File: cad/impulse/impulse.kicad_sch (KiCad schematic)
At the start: 0 parts

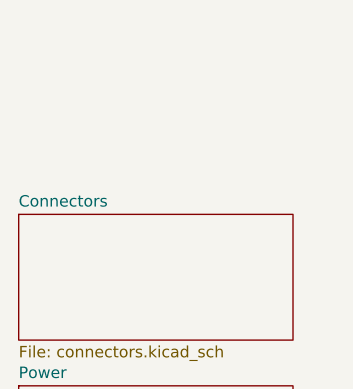
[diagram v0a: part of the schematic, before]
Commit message: Started Working on sensors. Made connectors for servos.
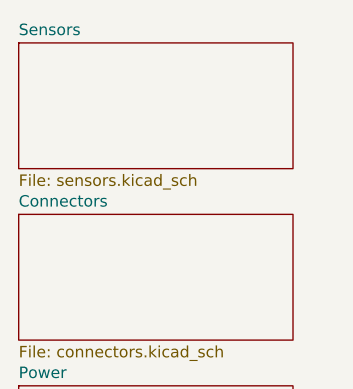
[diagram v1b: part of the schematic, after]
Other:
- added sheet Sensors (sensors.kicad_sch)
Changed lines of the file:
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@@
 (kicad_sch (version 20230121) (generator eeschema)
   (paper "A4")
+  (sheet (at 227.33 105.41) (size 30.48 13.97) (fields_autoplaced)
+    (stroke (width 0.1524) (type solid))
+    (fill (color 0 0 0 0.0000))
+    (property "Sheetname" "Sensors" (at 227.33 104.6984 0)
+      (effects (font (size 1.27 1.27)) (justify left bottom))
+    )
+    (property "Sheetfile" "sensors.kicad_sch" (at 227.33 119.9646 0)
+      (effects (font (size 1.27 1.27)) (justify left top))
+    )
+    (instances
+      (project "impulse"
+        (path "/eb4cfece-5fcb-437a-ac58-337ab6512039" (page "4"))
+      )
+    )
+  )
   (sheet (at 227.33 143.51) (size 30.48 13.97) (fields_autoplaced)
     (stroke (width 0.1524) (type solid))

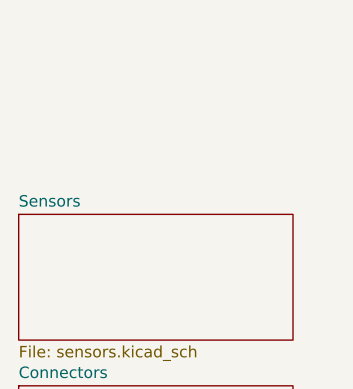
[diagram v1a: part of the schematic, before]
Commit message: Added IMU, button and led. Moved things around.
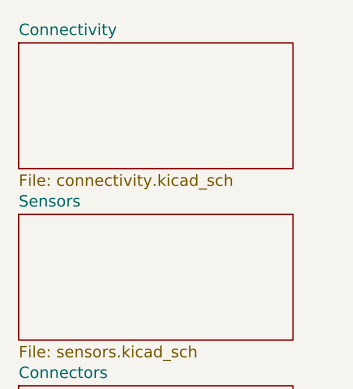
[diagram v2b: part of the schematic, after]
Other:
- added sheet Connectivity (connectivity.kicad_sch)
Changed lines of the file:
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@@
+    )
+  )
+  (sheet (at 227.33 86.36) (size 30.48 13.97) (fields_autoplaced)
+    (stroke (width 0.1524) (type solid))
+    (fill (color 0 0 0 0.0000))
+    (property "Sheetname" "Connectivity" (at 227.33 85.6484 0)
+      (effects (font (size 1.27 1.27)) (justify left bottom))
+    )
+    (property "Sheetfile" "connectivity.kicad_sch" (at 227.33 100.9146 0)
+      (effects (font (size 1.27 1.27)) (justify left top))
+    )
+    (instances
+      (project "impulse"
+        (path "/eb4cfece-5fcb-437a-ac58-337ab6512039" (page "5"))
+      )
     )
   )

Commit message: Finnished the design.
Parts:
- added C38, C39, C40, C44: 100n, symbol Device:C_Small
- added C41: 4u7, symbol Device:C_Small
- added C42: 10n, symbol Device:C_Small
- added C43, C45: 1u, symbol Device:C_Small
- added C46, C47: 10p, symbol Device:C_Small
- added J14: Conn_02x04_Counter_Clockwise, symbol Connector_Generic:Conn_02x04_Counter_Clockwise
- added R14, R15, R35, R36, R37: 0r, symbol Device:R_Small
- added U13: STM32G431CBUx, symbol MCU_ST_STM32G4:STM32G431CBUx
- added Y2: X252016MLB4SI, symbol Device:Crystal_GND24
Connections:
- new net: J14.2 (Pin_2), R14.2
- new net: J14.3 (Pin_3), R15.2
- new net: J14.5 (Pin_5), R37.1
- new net: J14.6 (Pin_6), R36.1
- new net: J14.7 (Pin_7), R35.1
- new net +3V3: C38.1, C39.1, C40.1, C41.1, C42.1, C43.1, C44.1, C45.1, J14.8 (Pin_8), U13.1 (VBAT), U13.20 (VREF+), U13.21 (VDDA), U13.23 (VDD), U13.35 (VDD), U13.48 (VDD)
- new net GND: C38.2, C39.2, C40.2, C41.2, C42.2, C43.2, C44.2, C45.2, C46.2, C47.2, J14.1 (Pin_1), J14.4 (Pin_4), U13.49 (VSS), Y2.2, Y2.4
- new net SD_cs: U13.32 (PA10)
- new net SD_miso: U13.40 (PC11)
- new net SD_mosi: U13.43 (PB5)
- new net SD_sck: U13.39 (PC10)
- new net button: R37.2, U13.7 (PG10)
- new net flash_cs: U13.25 (PB12)
- new net flash_miso: U13.27 (PB14)
- new net flash_mosi: U13.28 (PB15)
- new net flash_sck: U13.26 (PB13)
- new net fpc_gpio: U13.16 (PC4)
- new net fpc_rx: U13.24 (PB11)
- new net fpc_scl: U13.38 (PA15)
- new net fpc_sda: U13.47 (PB9)
- new net fpc_tx: U13.22 (PB10)
- new net i2c2_scl: U13.31 (PA9)
- new net i2c2_sda: U13.30 (PA8)
- new net led_b: U13.4 (PC15)
- new net led_g: U13.3 (PC14)
- new net led_r: U13.2 (PC13)
- new net pyro_0: U13.44 (PB6)
- new net pyro_1: U13.45 (PB7)
- new net pyro_2: U13.46 (PB8)
- new net pyro_3: U13.17 (PB0)
- new net servo_0: U13.8 (PA0)
- new net servo_1: U13.9 (PA1)
- new net servo_2: U13.10 (PA2)
- new net servo_3: U13.11 (PA3)
- new net servo_4: U13.29 (PC6)
- new net servo_5: U13.12 (PA4)
- new net stm_swclk: R15.1, U13.37 (PA14)
- new net stm_swdio: R14.1, U13.36 (PA13)
- new net stm_xta: C46.1, U13.5 (PF0), Y2.3
- new net stm_xtb: C47.1, U13.6 (PF1), Y2.1
- new net sx_miso: U13.14 (PA6)
- new net sx_mosi: U13.15 (PA7)
- new net sx_nss: U13.18 (PB1)
- new net sx_sck: U13.13 (PA5)
- new net usart2_rx: R35.2, U13.42 (PB4)
- new net usart2_tx: R36.2, U13.41 (PB3)
- new net usb_d+: U13.34 (PA12)
- new net usb_d-: U13.33 (PA11)
- new net vbat_sense: U13.19 (PB2)
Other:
- note added: "Debug Connector"
- note added: "Oscillator"
- note added: "VDD"
- note added: "VDDA"
- note added: "VREF+"
- company: (none) -> markbel
- title: (none) -> MCU

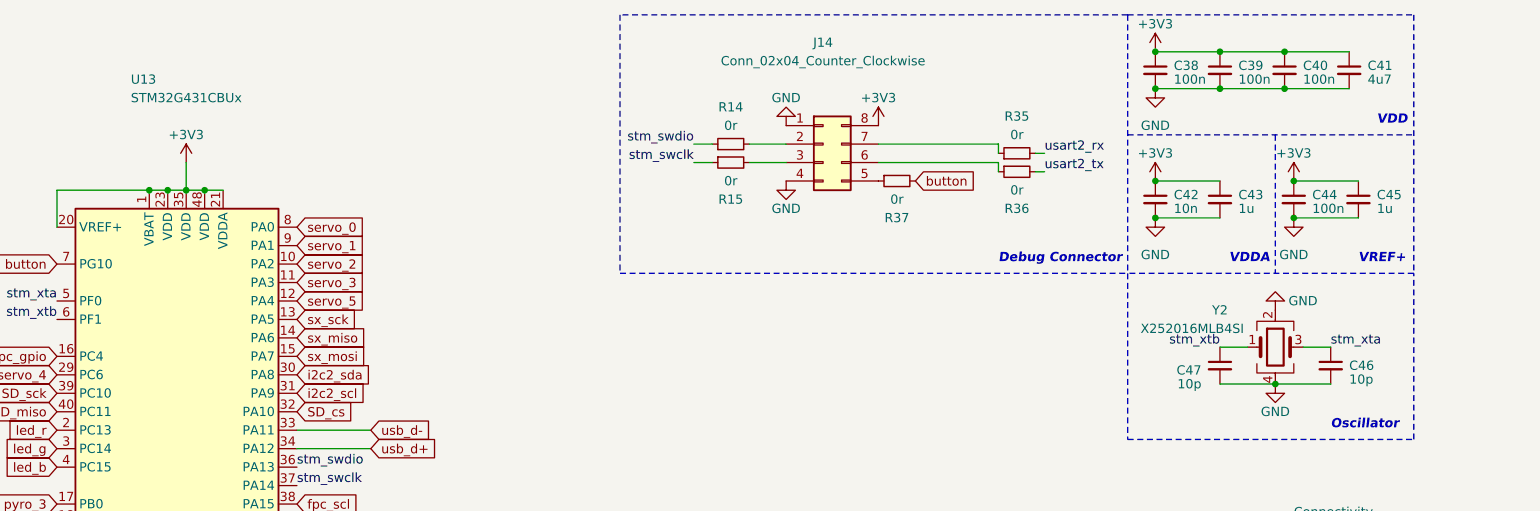
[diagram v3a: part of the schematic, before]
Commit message: Started working on BOM, did consolidation.
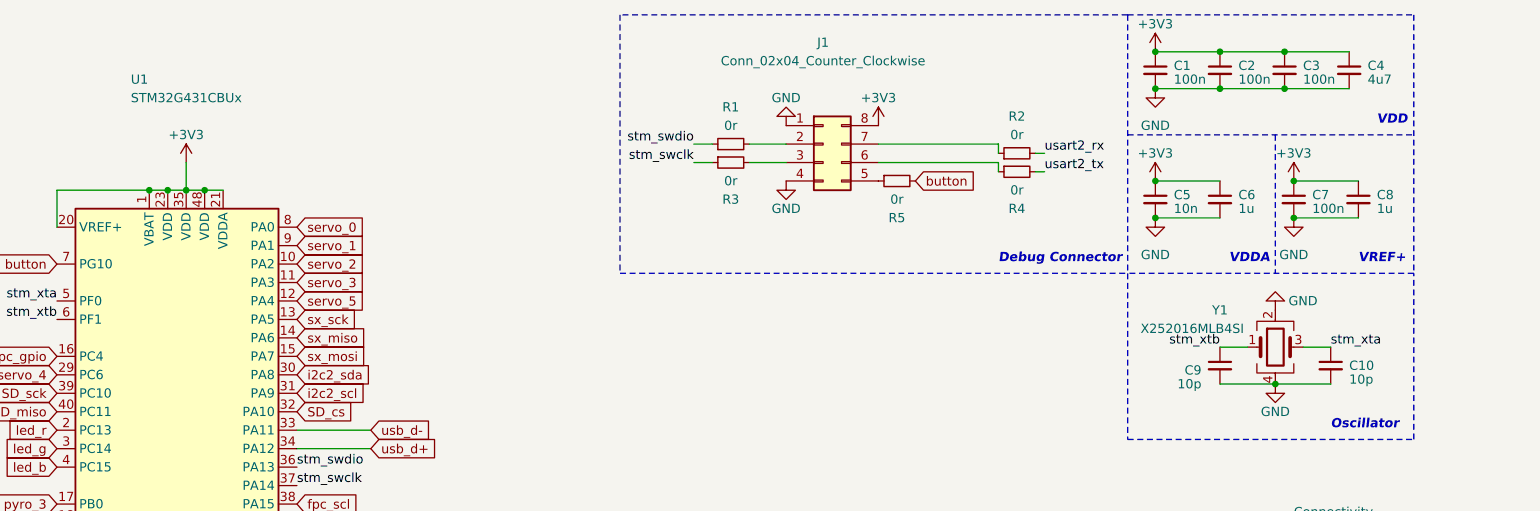
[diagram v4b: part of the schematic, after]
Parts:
- C1: renamed from C38; lcsc (none) -> C1525
- C10: renamed from C46; lcsc (none) -> C1545
- C2: renamed from C39; lcsc (none) -> C1525
- C3: renamed from C40; lcsc (none) -> C1525
- C4: renamed from C41; lcsc (none) -> C5360855
- C6: renamed from C43; lcsc (none) -> C167338
- C7: renamed from C44; lcsc (none) -> C1525
- C8: renamed from C45; lcsc (none) -> C167338
- C9: renamed from C47; lcsc (none) -> C1545
- J1: renamed from J14; lcsc (none) -> C2685182
- R1: renamed from R14; lcsc (none) -> C21376
- R2: renamed from R35; lcsc (none) -> C21376
- R3: renamed from R15; lcsc (none) -> C21376
- R4: renamed from R36; lcsc (none) -> C21376
- R5: renamed from R37; lcsc (none) -> C21376
- U1: renamed from U13; lcsc (none) -> C529356
- Y1: renamed from Y2; lcsc (none) -> C784073
- renumbered C42 to C5

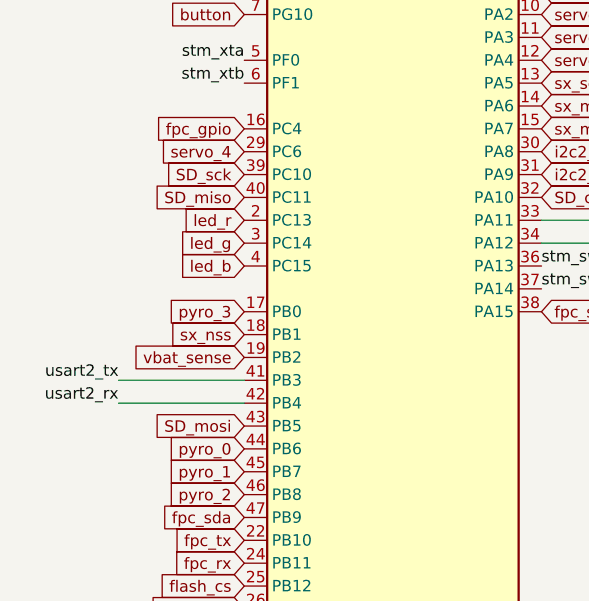
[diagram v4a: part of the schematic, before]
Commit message: Finished with schematic, starting to route traces.
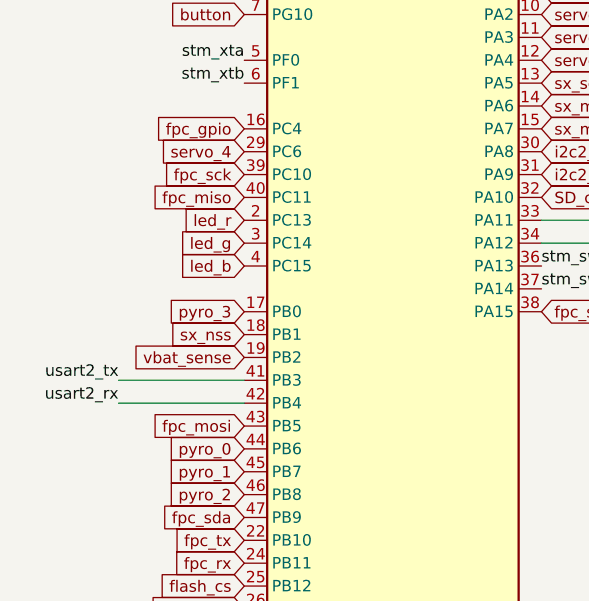
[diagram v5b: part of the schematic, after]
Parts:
- C1, C10, C2, C3, C7, C9: footprint (none) -> Capacitor_SMD:C_0402_1005Metric
- C4, C6, C8: footprint (none) -> Capacitor_SMD:C_0603_1608Metric
- C5: footprint (none) -> Capacitor_SMD:C_0603_1608Metric; lcsc (none) -> C525264
- J1: footprint (none) -> Connector_PinHeader_1.27mm:PinHeader_2x04_P1.27mm_Vertical
- R1, R2, R3, R4, R5: footprint (none) -> Resistor_SMD:R_0402_1005Metric
- U1: footprint (none) -> Package_DFN_QFN:QFN-48-1EP_7x7mm_P0.5mm_EP5.6x5.6mm
- Y1: footprint (none) -> Crystal:Crystal_SMD_2520-4Pin_2.5x2.0mm
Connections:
- net SD_miso renamed fpc_miso
- net SD_mosi renamed fpc_mosi
- net SD_sck renamed fpc_sck
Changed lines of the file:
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@@
     )
   )
-  (global_label "SD_mosi" (shape input) (at 80.01 99.06 180) (fields_autoplaced)
+  (global_label "fpc_mosi" (shape input) (at 80.01 99.06 180) (fields_autoplaced)
     (effects (font (size 1.27 1.27)) (justify right))
-    (property "Intersheetrefs" "${INTERSHEET_REFS}" (at 69.1819 99.06 0)
+    (property "Intersheetrefs" "${INTERSHEET_REFS}" (at 68.6981 99.06 0)
       (effects (font (size 1.27 1.27)) (justify right) hide)
     )
@@
     )
   )
-  (global_label "SD_sck" (shape input) (at 80.01 71.12 180) (fields_autoplaced)
+  (global_label "fpc_sck" (shape input) (at 80.01 71.12 180) (fields_autoplaced)
     (effects (font (size 1.27 1.27)) (justify right))
-    (property "Intersheetrefs" "${INTERSHEET_REFS}" (at 70.5123 71.12 0)
+    (property "Intersheetrefs" "${INTERSHEET_REFS}" (at 70.0285 71.12 0)
       (effects (font (size 1.27 1.27)) (justify right) hide)
     )
@@
     )
   )
-  (global_label "SD_miso" (shape input) (at 80.01 73.66 180) (fields_autoplaced)
+  (global_label "fpc_miso" (shape input) (at 80.01 73.66 180) (fields_autoplaced)
     (effects (font (size 1.27 1.27)) (justify right))
-    (property "Intersheetrefs" "${INTERSHEET_REFS}" (at 69.1819 73.66 0)
+    (property "Intersheetrefs" "${INTERSHEET_REFS}" (at 68.6981 73.66 0)
       (effects (font (size 1.27 1.27)) (justify right) hide)
     )
@@
       (effects (font (size 1.27 1.27)))
     )
-    (property "Footprint" "" (at 247.65 64.77 0)
+    (property "Footprint" "Crystal:Crystal_SMD_2520-4Pin_2.5x2.0mm" (at 247.65 64.77 0)
       (effects (font (size 1.27 1.27)) hide)
     )
@@
       (effects (font (size 1.27 1.27)) (justify left))
     )
-    (property "Footprint" "" (at 82.55 129.54 0)
+    (property "Footprint" "Package_DFN_QFN:QFN-48-1EP_7x7mm_P0.5mm_EP5.6x5.6mm" (at 82.55 129.54 0)
       (effects (font (size 1.27 1.27)) (justify right) hide)
     )
@@
       (effects (font (size 1.27 1.27)))
     )
-    (property "Footprint" "" (at 185.42 36.83 0)
+    (property "Footprint" "Connector_PinHeader_1.27mm:PinHeader_2x04_P1.27mm_Vertical" (at 185.42 36.83 0)
       (effects (font (size 1.27 1.27)) hide)
     )
@@
       (effects (font (size 1.27 1.27)) (justify left))
     )
-    (property "Footprint" "" (at 231.14 44.45 0)
+    (property "Footprint" "Capacitor_SMD:C_0603_1608Metric" (at 231.14 44.45 0)
       (effects (font (size 1.27 1.27)) hide)
     )
@@
       (effects (font (size 1.27 1.27)) hide)
     )
-    (property "lcsc" "" (at 231.14 44.45 0)
+    (property "lcsc" "C525264" (at 231.14 44.45 0)
       (effects (font (size 1.27 1.27)) hide)
     )
@@
       (effects (font (size 1.27 1.27)))
     )
-    (property "Footprint" "" (at 172.72 36.83 0)
+    (property "Footprint" "Resistor_SMD:R_0402_1005Metric" (at 172.72 36.83 0)
       (effects (font (size 1.27 1.27)) hide)
     )
@@
       (effects (font (size 1.27 1.27)))
     )
-    (property "Footprint" "" (at 172.72 39.37 0)
+    (property "Footprint" "Resistor_SMD:R_0402_1005Metric" (at 172.72 39.37 0)
       (effects (font (size 1.27 1.27)) hide)
     )
@@
       (effects (font (size 1.27 1.27)))
     )
-    (property "Footprint" "" (at 212.09 40.64 0)
+    (property "Footprint" "Resistor_SMD:R_0402_1005Metric" (at 212.09 40.64 0)
       (effects (font (size 1.27 1.27)) hide)
     )
@@
       (effects (font (size 1.27 1.27)))
     )
-    (property "Footprint" "" (at 195.58 41.91 0)
+    (property "Footprint" "Resistor_SMD:R_0402_1005Metric" (at 195.58 41.91 0)
       (effects (font (size 1.27 1.27)) hide)
     )
@@
       (effects (font (size 1.27 1.27)) (justify left))
     )
-    (property "Footprint" "" (at 240.03 26.67 0)
+    (property "Footprint" "Capacitor_SMD:C_0402_1005Metric" (at 240.03 26.67 0)
       (effects (font (size 1.27 1.27)) hide)
     )
@@
       (effects (font (size 1.27 1.27)) (justify left))
     )
-    (property "Footprint" "" (at 248.92 26.67 0)
+    (property "Footprint" "Capacitor_SMD:C_0402_1005Metric" (at 248.92 26.67 0)
       (effects (font (size 1.27 1.27)) hide)
     )
@@
       (effects (font (size 1.27 1.27)))
     )
-    (property "Footprint" "" (at 212.09 38.1 0)
+    (property "Footprint" "Resistor_SMD:R_0402_1005Metric" (at 212.09 38.1 0)
       (effects (font (size 1.27 1.27)) hide)
     )
@@
       (effects (font (size 1.27 1.27)) (justify left))
     )
-    (property "Footprint" "" (at 255.27 67.31 0)
+    (property "Footprint" "Capacitor_SMD:C_0402_1005Metric" (at 255.27 67.31 0)
       (effects (font (size 1.27 1.27)) hide)
     )
@@
       (effects (font (size 1.27 1.27)) (justify left))
     )
-    (property "Footprint" "" (at 250.19 44.45 0)
+    (property "Footprint" "Capacitor_SMD:C_0402_1005Metric" (at 250.19 44.45 0)
       (effects (font (size 1.27 1.27)) hide)
     )
@@
       (effects (font (size 1.27 1.27)) (justify left))
     )
-    (property "Footprint" "" (at 259.08 44.45 0)
+    (property "Footprint" "Capacitor_SMD:C_0603_1608Metric" (at 259.08 44.45 0)
       (effects (font (size 1.27 1.27)) hide)
     )
@@
       (effects (font (size 1.27 1.27)) (justify left))
     )
-    (property "Footprint" "" (at 257.81 26.67 0)
+    (property "Footprint" "Capacitor_SMD:C_0603_1608Metric" (at 257.81 26.67 0)
       (effects (font (size 1.27 1.27)) hide)
     )
@@
       (effects (font (size 1.27 1.27)) (justify left))
     )
-    (property "Footprint" "" (at 240.03 44.45 0)
+    (property "Footprint" "Capacitor_SMD:C_0603_1608Metric" (at 240.03 44.45 0)
       (effects (font (size 1.27 1.27)) hide)
     )
@@
       (effects (font (size 1.27 1.27)) (justify left))
     )
-    (property "Footprint" "" (at 240.03 67.31 0)
+    (property "Footprint" "Capacitor_SMD:C_0402_1005Metric" (at 240.03 67.31 0)
       (effects (font (size 1.27 1.27)) hide)
     )
@@
       (effects (font (size 1.27 1.27)) (justify left))
     )
-    (property "Footprint" "" (at 231.14 26.67 0)
-      (effects (font (size 1.27 1.27)) hide)
-    )
+    (property "Footprint" "Capacitor_SMD:C_0402_1005Metric" (at 231.14 26.67 0)
+      (effects (font (size 1.27 1.27)) hide)
+    )
